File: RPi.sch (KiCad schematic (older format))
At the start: 3 parts, among them U4 ECP5, X3 RaspberryPiConnector

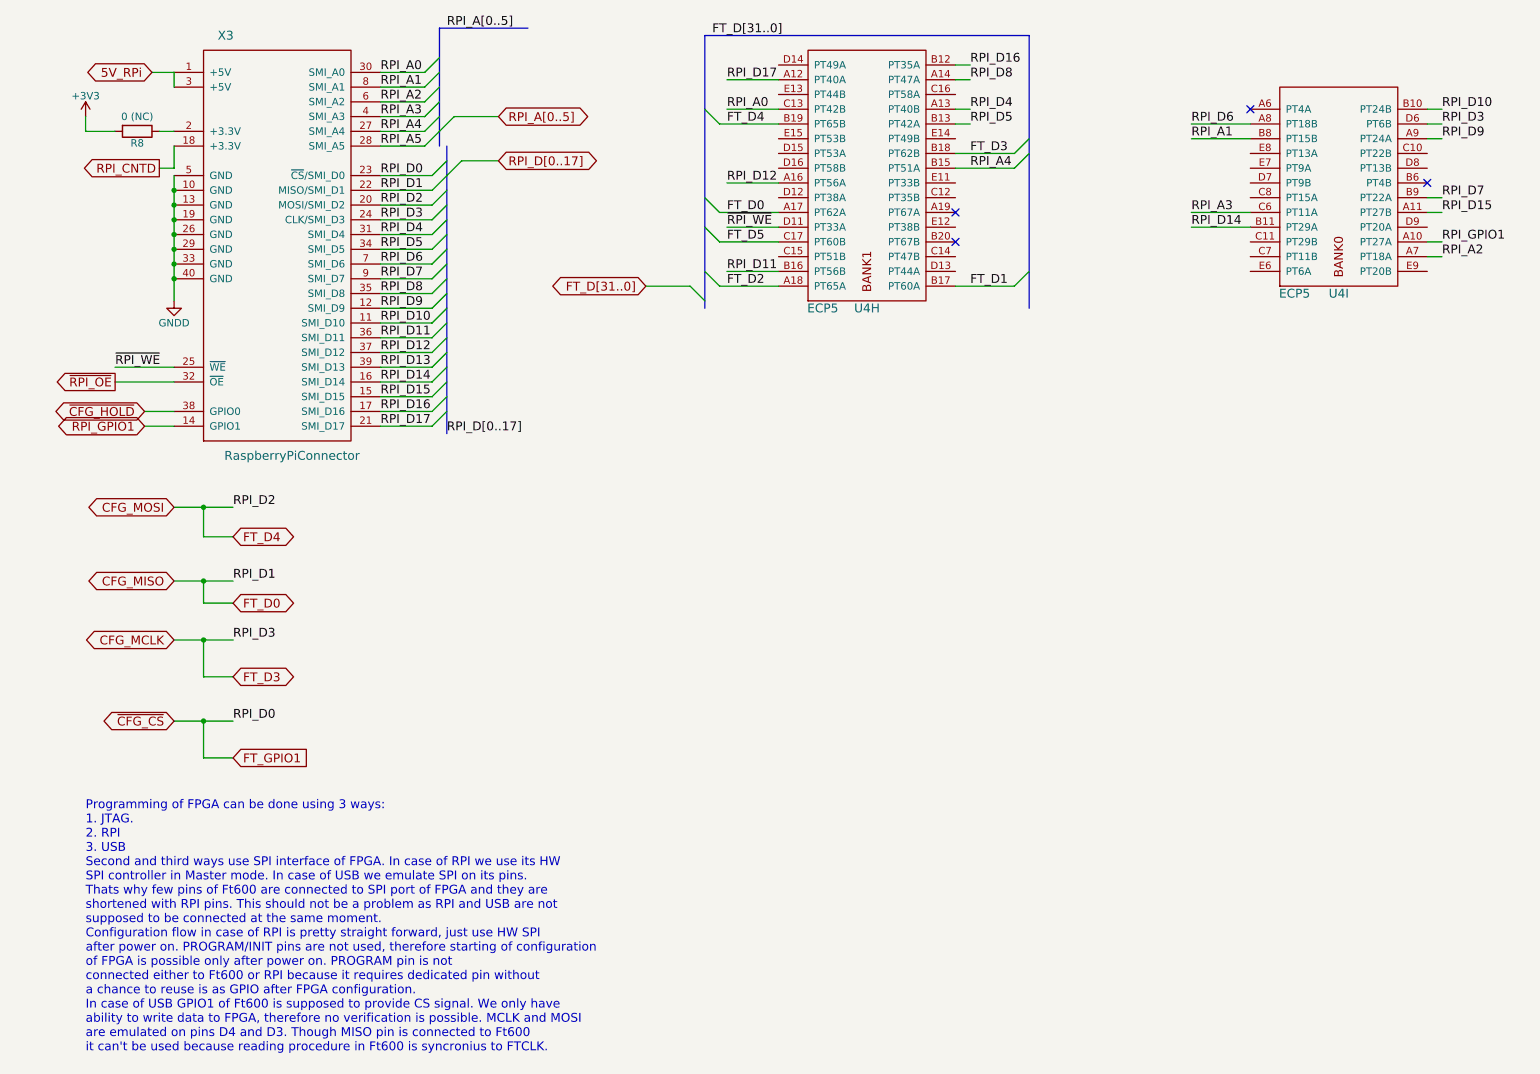
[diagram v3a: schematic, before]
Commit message: Preliminary placing top layer of RF
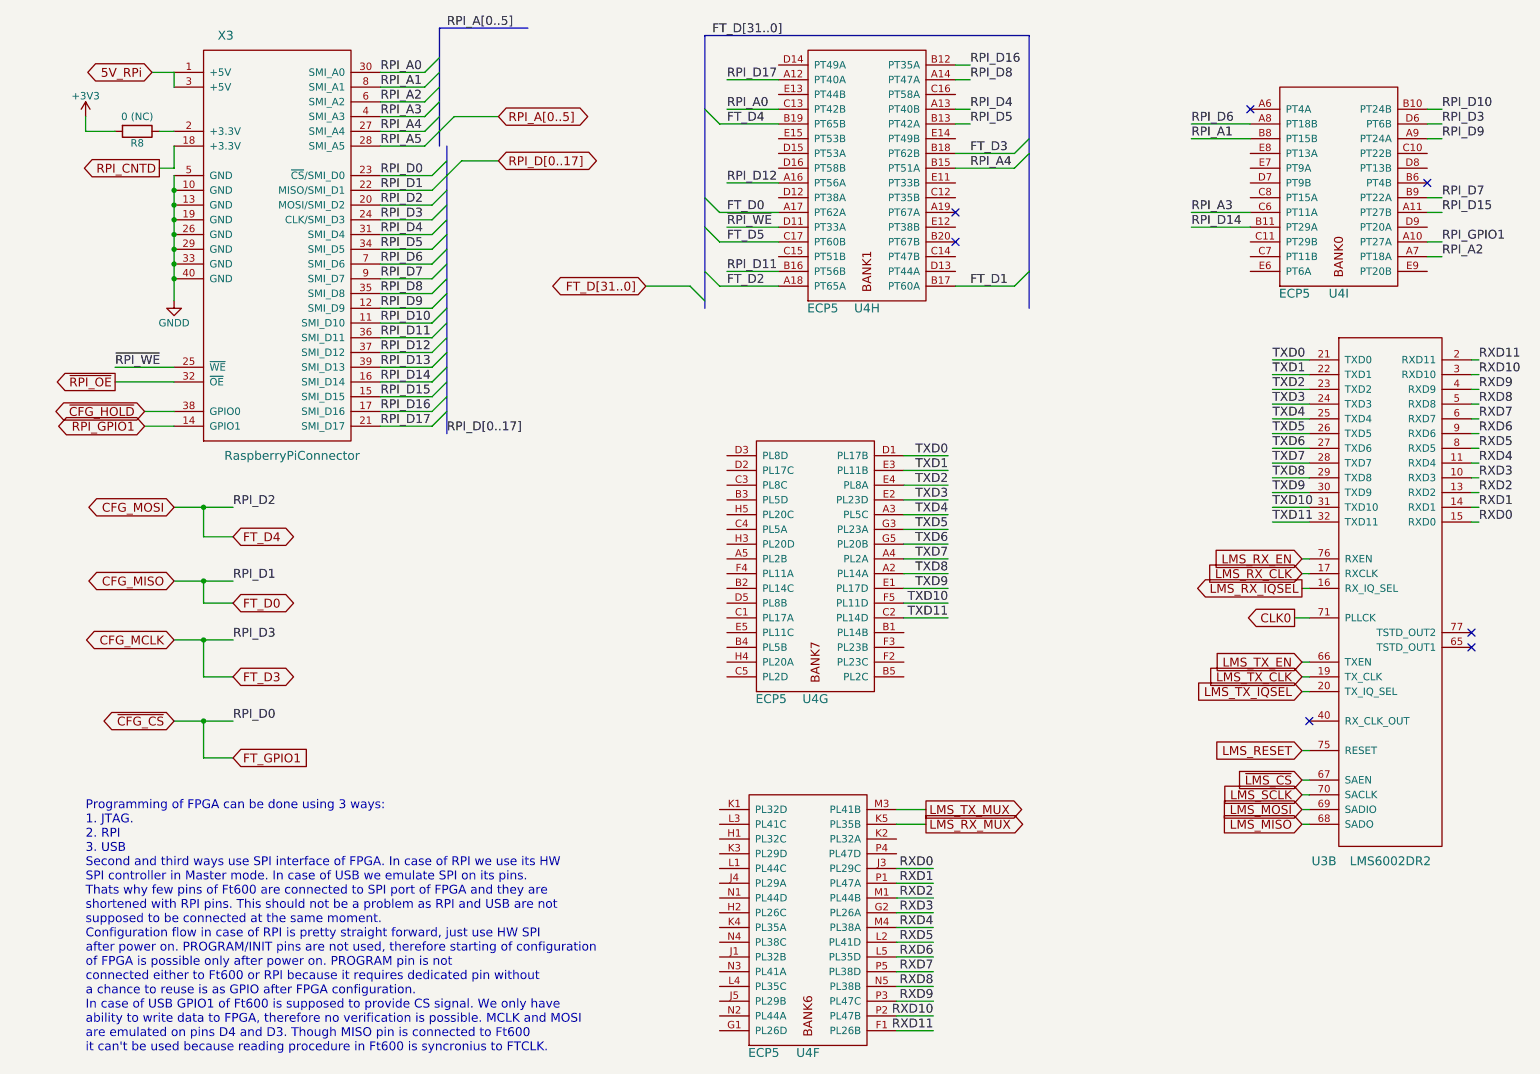
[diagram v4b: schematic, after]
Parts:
- added U3: LMS6002DR2, sdr-foots:DQFN-120_via_off_pad, symbol LMS6002DR2
- added unit 6 of U4
- added unit 7 of U4
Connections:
- new net CLK0: U3.71 (PLLCK)
- new net LMS_MISO: U3.68 (SADO)
- new net LMS_MOSI: U3.69 (SADIO)
- new net LMS_RESET: U3.75 (RESET)
- new net LMS_RX_CLK: U3.17 (RXCLK)
- new net LMS_RX_EN: U3.76 (RXEN)
- new net LMS_RX_IQSEL: U3.16 (RX_IQ_SEL)
- new net LMS_RX_MUX: U4.K5 (PL35B)
- new net LMS_SCLK: U3.70 (SACLK)
- new net LMS_TX_CLK: U3.19 (TX_CLK)
- new net LMS_TX_EN: U3.66 (TXEN)
- new net LMS_TX_IQSEL: U3.20 (TX_IQ_SEL)
- new net LMS_TX_MUX: U4.M3 (PL41B)
- new net RXD0: U3.15 (RXD0), U4.J3 (PL29C)
- new net RXD1: U3.14 (RXD1), U4.P1 (PL47A)
- new net RXD10: U3.3 (RXD10), U4.P2 (PL47B)
- new net RXD11: U3.2 (RXD11), U4.F1 (PL26B)
- new net RXD2: U3.13 (RXD2), U4.M1 (PL44B)
- new net RXD3: U3.10 (RXD3), U4.G2 (PL26A)
- new net RXD4: U3.11 (RXD4), U4.M4 (PL38A)
- new net RXD5: U3.8 (RXD5), U4.L2 (PL41D)
- new net RXD6: U3.9 (RXD6), U4.L5 (PL35D)
- new net RXD7: U3.6 (RXD7), U4.P5 (PL38D)
- new net RXD8: U3.5 (RXD8), U4.N5 (PL38B)
- new net RXD9: U3.4 (RXD9), U4.P3 (PL47C)
- new net TXD0: U3.21 (TXD0), U4.D1 (PL17B)
- new net TXD1: U3.22 (TXD1), U4.E3 (PL11B)
- new net TXD10: U3.31 (TXD10), U4.F5 (PL11D)
- new net TXD11: U3.32 (TXD11), U4.C2 (PL14D)
- new net TXD2: U3.23 (TXD2), U4.E4 (PL8A)
- new net TXD3: U3.24 (TXD3), U4.E2 (PL23D)
- new net TXD4: U3.25 (TXD4), U4.A3 (PL5C)
- new net TXD5: U3.26 (TXD5), U4.G3 (PL23A)
- new net TXD6: U3.27 (TXD6), U4.G5 (PL20B)
- new net TXD7: U3.28 (TXD7), U4.A4 (PL2A)
- new net TXD8: U3.29 (TXD8), U4.A2 (PL14A)
- new net TXD9: U3.30 (TXD9), U4.E1 (PL17D)
- new net ~LMS_CS: U3.67 (SAEN)
- no-connect marks 4 -> 7

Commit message: Placement of RF is on going.
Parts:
- U4: footprint (none) -> sdr-foots:ECP5_381
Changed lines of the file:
@@
 F 0 "U4" H 5700 7500 60  0000 C CNN
 F 1 "ECP5" H 5400 7500 60  0000 C CNN
-F 2 "" H 3750 8100 60  0001 C CNN
+F 2 "sdr-foots:ECP5_381" H 3750 8100 60  0001 C CNN
 F 3 "" H 3750 8100 60  0001 C CNN
 	6    5300 7550
@@
 F 0 "U4" H 5750 5100 60  0000 C CNN
 F 1 "ECP5" H 5450 5100 60  0000 C CNN
-F 2 "" H 3800 5700 60  0001 C CNN
+F 2 "sdr-foots:ECP5_381" H 3800 5700 60  0001 C CNN
 F 3 "" H 3800 5700 60  0001 C CNN
 	7    5350 5150
